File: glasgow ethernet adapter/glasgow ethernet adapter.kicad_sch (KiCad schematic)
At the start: 55 parts, among them J1 Glasgow Port, J2 RJ45_Amphenol_RJMG201K21120FR, U1 MxL86110, Y1 25 MHz

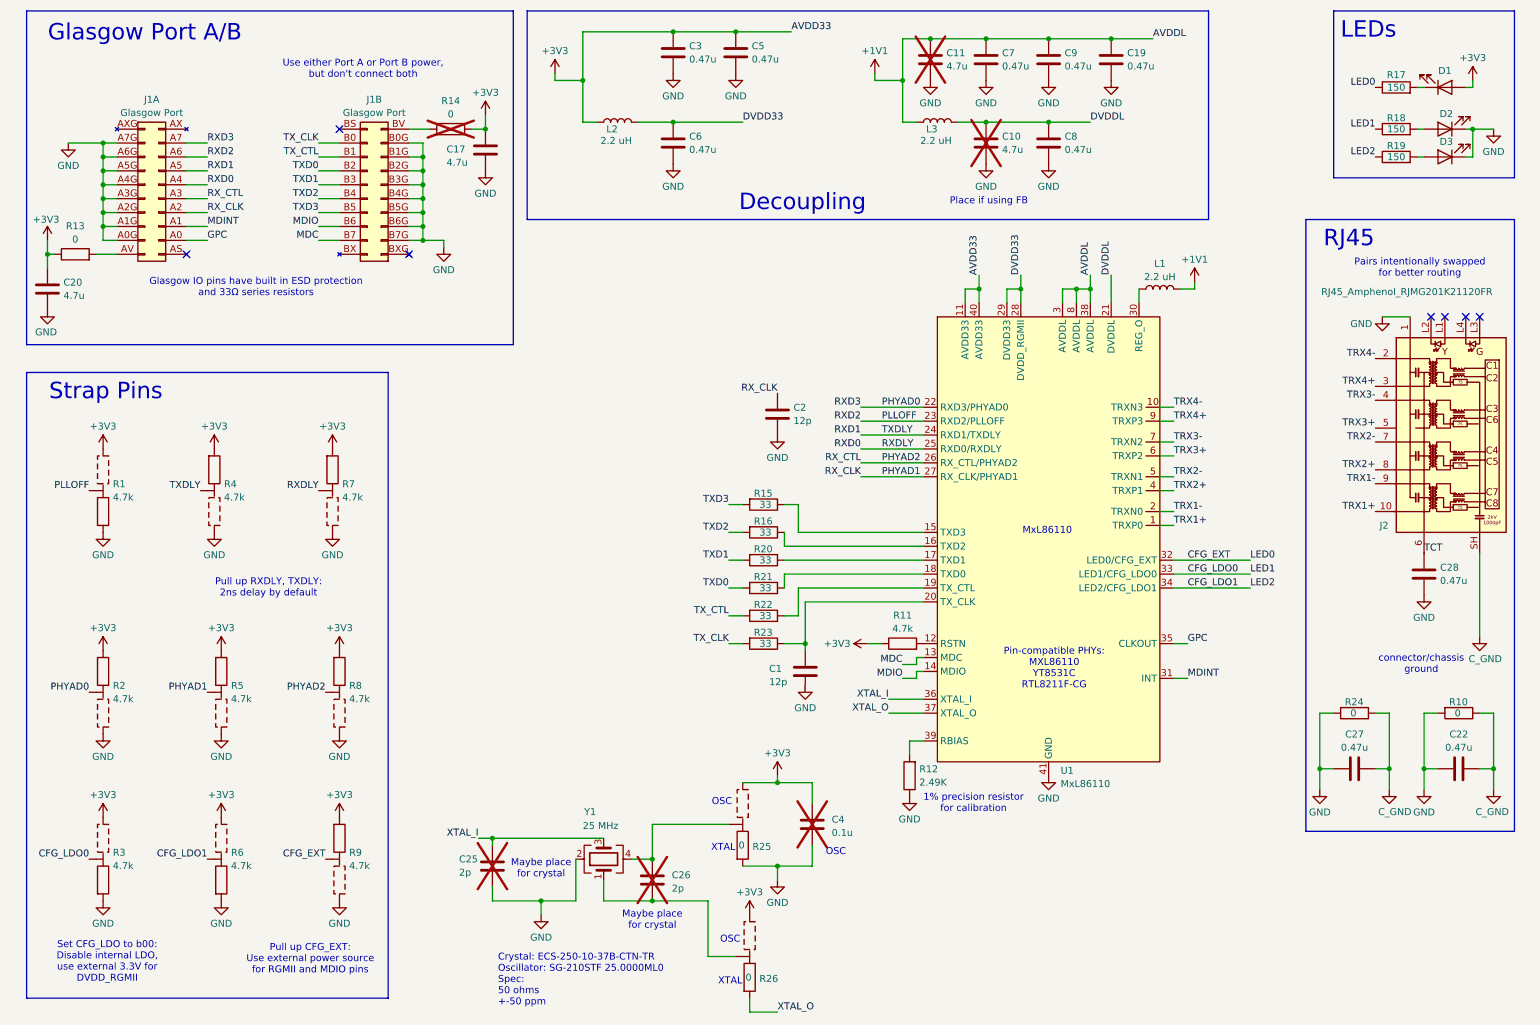
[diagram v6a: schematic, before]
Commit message: redo power + decoupling
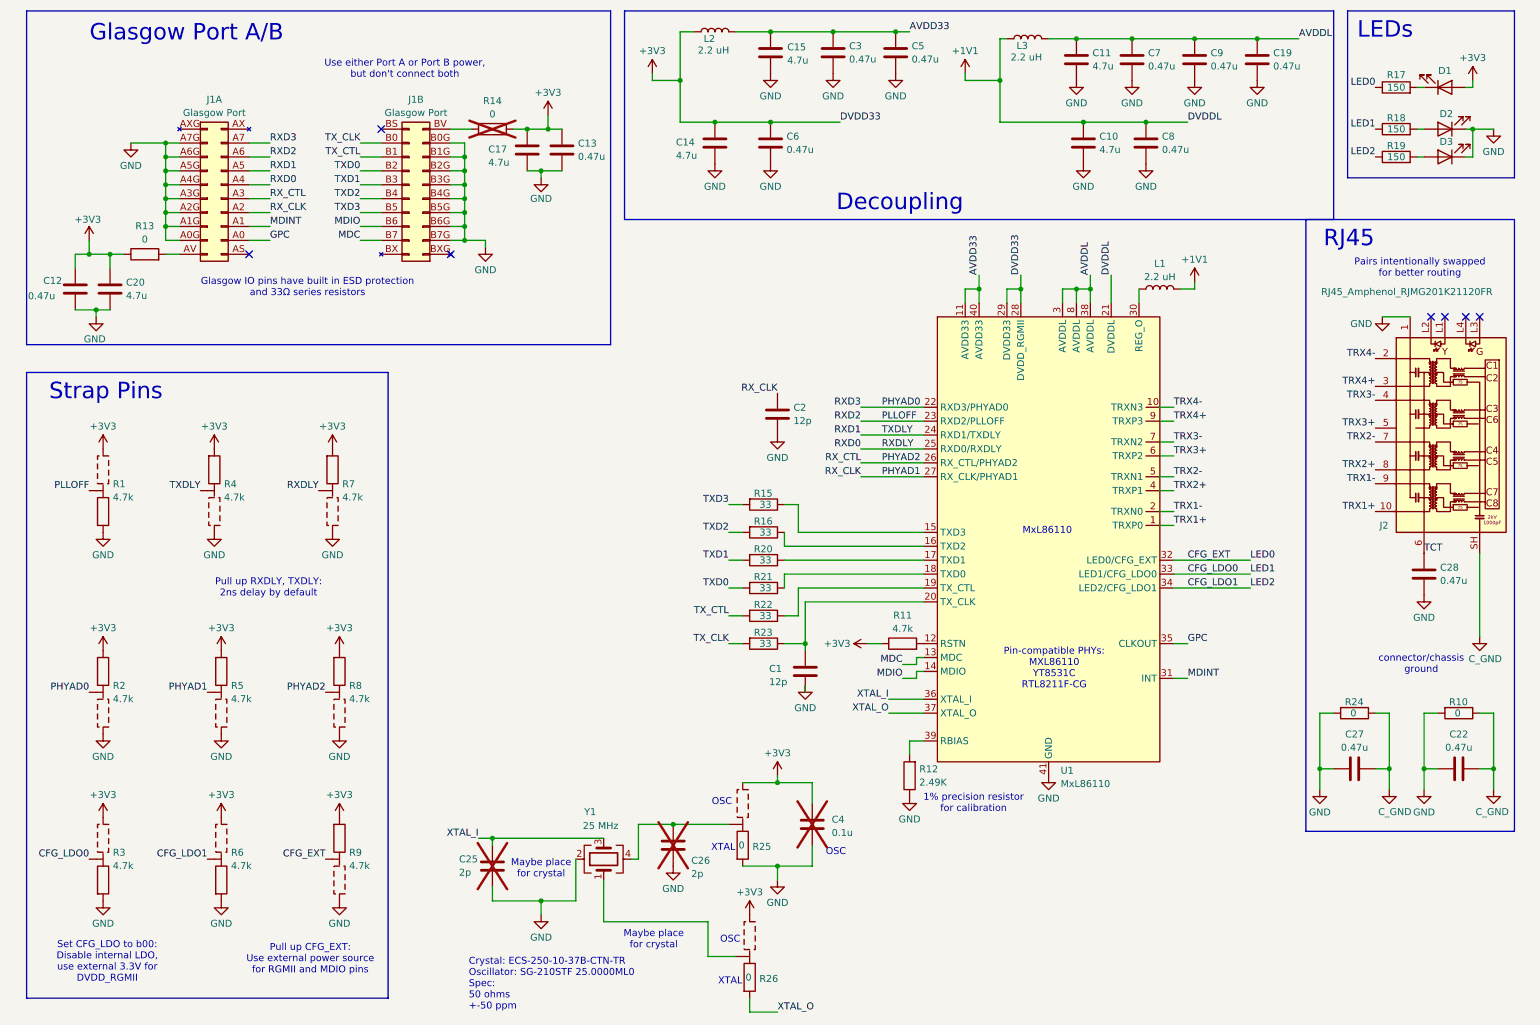
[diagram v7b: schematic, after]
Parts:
- added C12, C13: 0.47u, Capacitor_SMD:C_0402_1005Metric, symbol Device:C
- added C14, C15: 4.7u, Capacitor_SMD:C_1206_3216Metric, symbol Device:C
- C10, C11: now fitted
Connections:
- net +1V1: now also C10.1, C8.1, U1.21 (DVDDL); no longer C11.1, C19.1, C7.1, C9.1, U1.3 (AVDDL), U1.38 (AVDDL), U1.8 (AVDDL)
- net +3V3: now also C6.1, U1.28 (DVDD_RGMII), U1.29 (DVDD33), C12.1, C13.1, C14.1; no longer C3.1, C5.1, U1.11 (AVDD33), U1.40 (AVDD33)
- net GND: now also C26.2, C12.2, C13.2, C14.2, C15.2
- net at R26.2, Y1.1: no longer C26.2
- removed net DVDD33: C6.1, L2.2, U1.28 (DVDD_RGMII), U1.29 (DVDD33)
- removed net DVDDL: C10.1, C8.1, L3.2, U1.21 (DVDDL)
- new net AVDD33: C15.1, C3.1, C5.1, L2.2, U1.11 (AVDD33), U1.40 (AVDD33)
- new net AVDDL: C11.1, C19.1, C7.1, C9.1, L3.2, U1.3 (AVDDL), U1.38 (AVDDL), U1.8 (AVDDL)
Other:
- note removed: "Place if using FB"
- moved on the sheet: C17, C19, C20, C26, C3, C5, C6, C7, C8, C9, J1A, J1B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

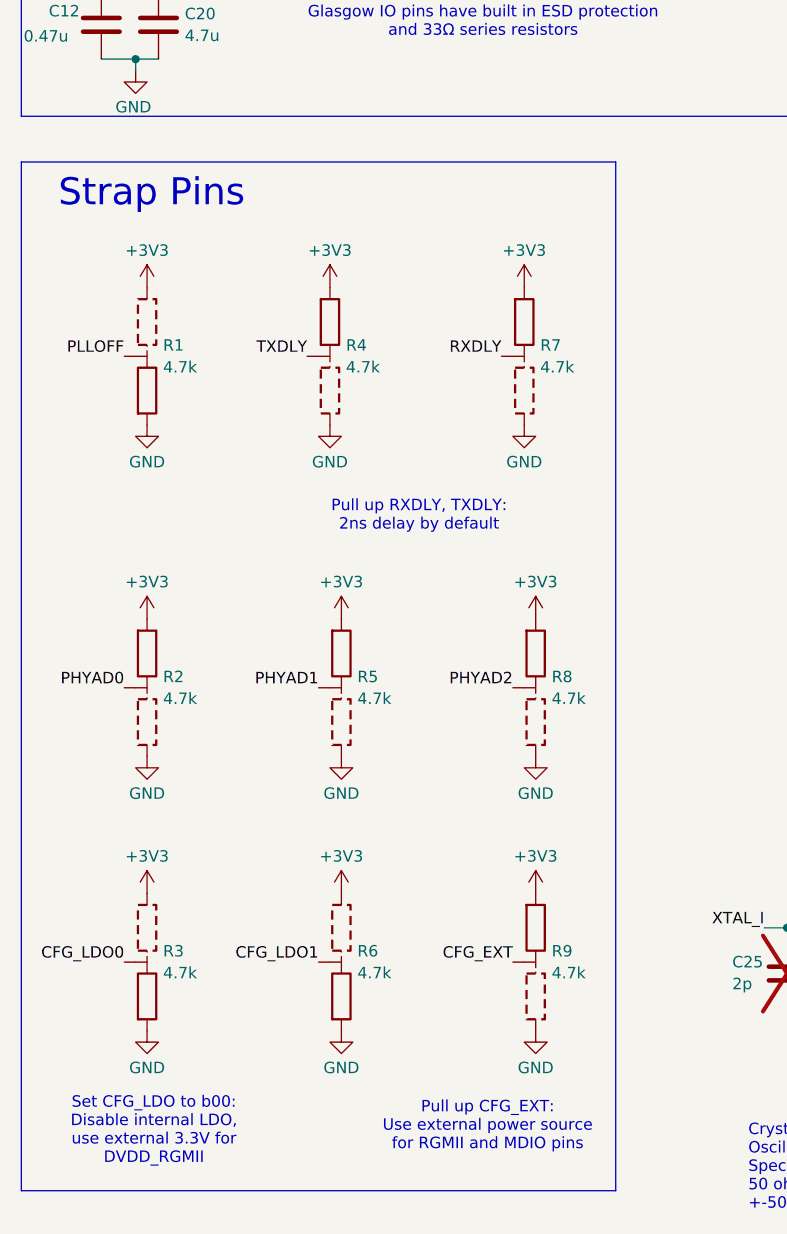
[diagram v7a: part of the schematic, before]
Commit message: remove configurable pulls on LEDs
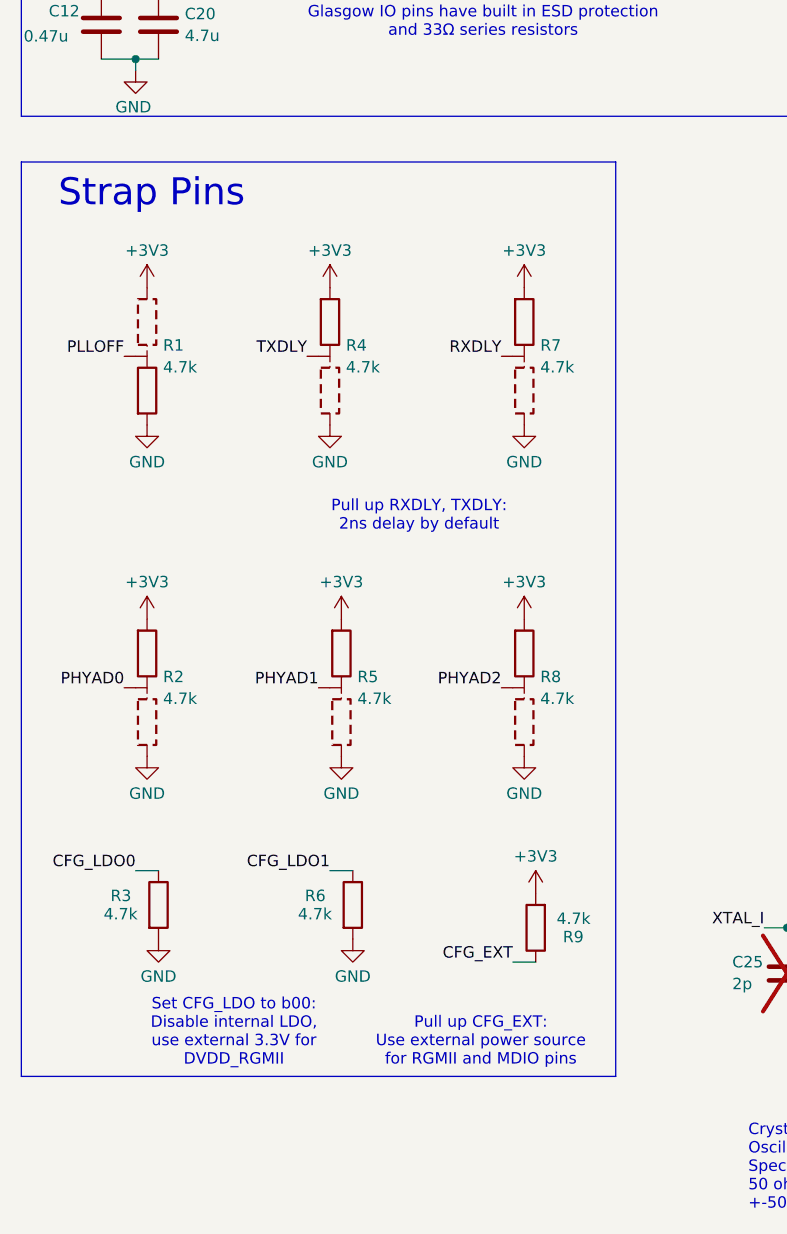
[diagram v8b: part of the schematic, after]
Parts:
- removed R3, R6, R9: 4.7k, glasgow:R-3-Way_0402_1005Metric, symbol glasgow:R-3-way
- added R3, R6, R9: 4.7k, Resistor_SMD:R_0402_1005Metric, symbol Device:R
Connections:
- net +3V3: now also R9.2
- net CFG_EXT: now also R9.1
- net CFG_LDO0: now also R3.1
- net CFG_LDO1: now also R6.1
- net GND: now also R3.2, R6.2
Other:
- moved on the sheet: R8
